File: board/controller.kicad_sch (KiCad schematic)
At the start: 4 parts, among them U1 MCP2515-xSO, Y1 20MhZ

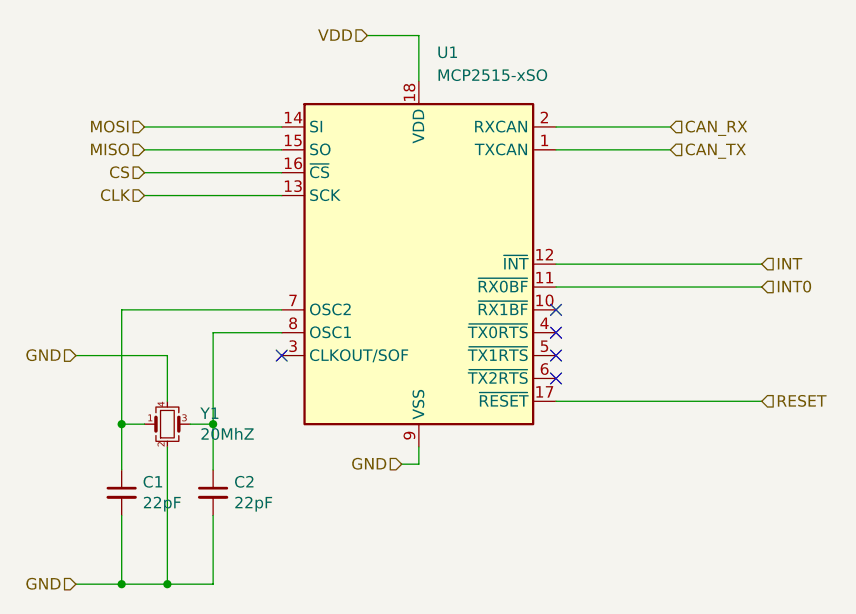
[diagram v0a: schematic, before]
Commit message: updated to kicad 8.0 and 20pin tssop
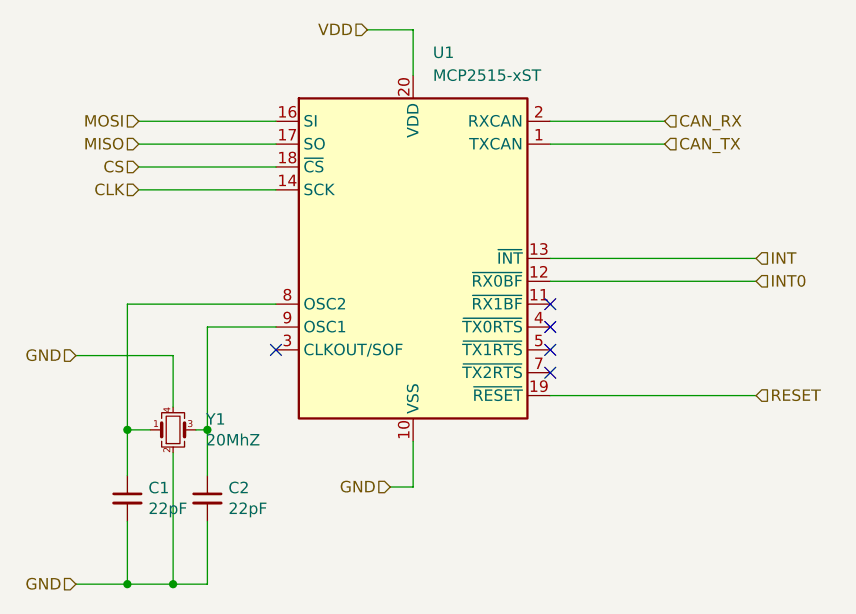
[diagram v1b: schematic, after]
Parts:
- removed U1: MCP2515-xSO, Package_SO:SOIC-18W_7.5x11.6mm_P1.27mm, symbol Interface_CAN_LIN:MCP2515-xSO
- added U1: MCP2515-xST, Package_SO:TSSOP-20_4.4x6.5mm_P0.65mm, symbol Interface_CAN_LIN:MCP2515-xST
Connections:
- net CAN_RX: now also U1.2 (RXCAN)
- net CAN_TX: now also U1.1 (TXCAN)
- net CLK: now also U1.14 (SCK)
- net CS: now also U1.18 (~{CS})
- net GND: now also U1.10 (VSS)
- net INT: now also U1.13 (~{INT})
- net INT0: now also U1.12 (~{RX0BF})
- net MISO: now also U1.17 (SO)
- net MOSI: now also U1.16 (SI)
- net RESET: now also U1.19 (~{RESET})
- net VDD: now also U1.20 (VDD)
- net at C1.1, Y1.1: now also U1.8 (OSC2)
- net at C2.1, Y1.3: now also U1.9 (OSC1)
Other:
- moved on the sheet: C1, C2, Y1

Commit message: added lcsc part numbers
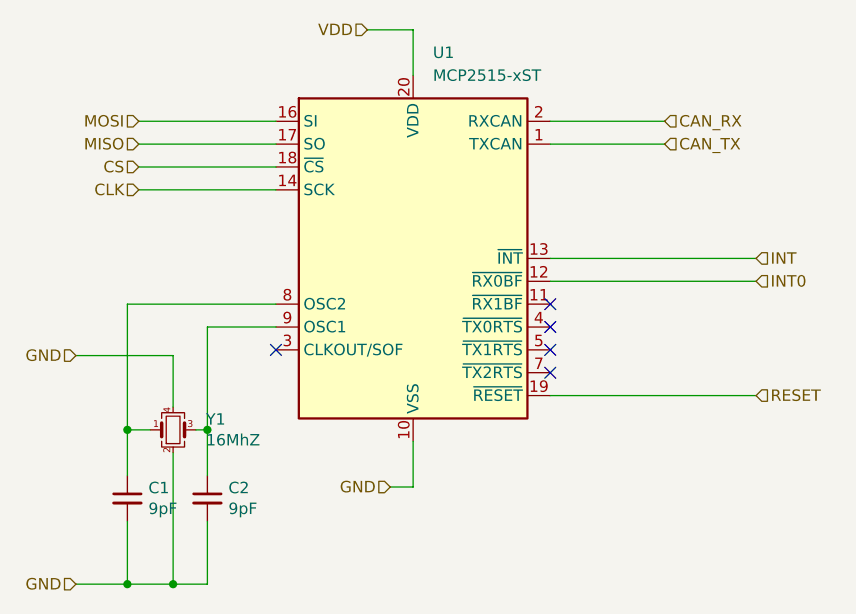
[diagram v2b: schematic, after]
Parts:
- C1, C2: value 22pF -> 9pF; lcsc (none) -> C1634
- U1: lcsc (none) -> C185941
- Y1: value 20MhZ -> 16MhZ; lcsc (none) -> C13738
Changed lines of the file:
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@@
       (effects (font (size 1.27 1.27)) (justify left))
     )
-    (property "Value" "20MhZ" (at 186.5376 101.473 0)
+    (property "Value" "16MhZ" (at 186.5376 101.473 0)
       (effects (font (size 1.27 1.27)) (justify left))
     )
@@
     )
     (property "MPN" "ECS-200-18-33-JGN-TR" (at 182.88 100.33 0)
+      (effects (font (size 1.27 1.27)) hide)
+    )
+    (property "lcsc" "C13738" (at 182.88 100.33 0)
       (effects (font (size 1.27 1.27)) hide)
     )
@@
       (effects (font (size 1.27 1.27)) (justify left))
     )
-    (property "Value" "22pF" (at 180.1368 109.093 0)
+    (property "Value" "9pF" (at 180.1368 109.093 0)
       (effects (font (size 1.27 1.27)) (justify left))
     )
@@
     )
     (property "Voltage" "6.3V" (at 177.8 107.95 0)
+      (effects (font (size 1.27 1.27)) hide)
+    )
+    (property "lcsc" "C1634" (at 177.8 107.95 0)
       (effects (font (size 1.27 1.27)) hide)
     )
@@
       (effects (font (size 1.27 1.27)) (justify right))
     )
-    (property "Value" "22pF" (at 189.0268 109.093 0)
+    (property "Value" "9pF" (at 189.0268 109.093 0)
       (effects (font (size 1.27 1.27)) (justify right))
     )
@@
     )
     (property "Voltage" "6.3V" (at 186.69 107.95 0)
+      (effects (font (size 1.27 1.27)) hide)
+    )
+    (property "lcsc" "C1634" (at 186.69 107.95 0)
       (effects (font (size 1.27 1.27)) hide)
     )
@@
       (effects (font (size 1.27 1.27)) hide)
     )
+    (property "lcsc" "C185941" (at 209.55 81.28 0)
+      (effects (font (size 1.27 1.27)) hide)
+    )
